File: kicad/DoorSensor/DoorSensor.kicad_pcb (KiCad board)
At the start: 2 copper layers, 29.7 x 38.6 mm, 11 parts, among them J1 AVR-ISP-6, J3 ADXL345 Module, U1 ATtiny44A-P, U2 NRF24L01_Breakout

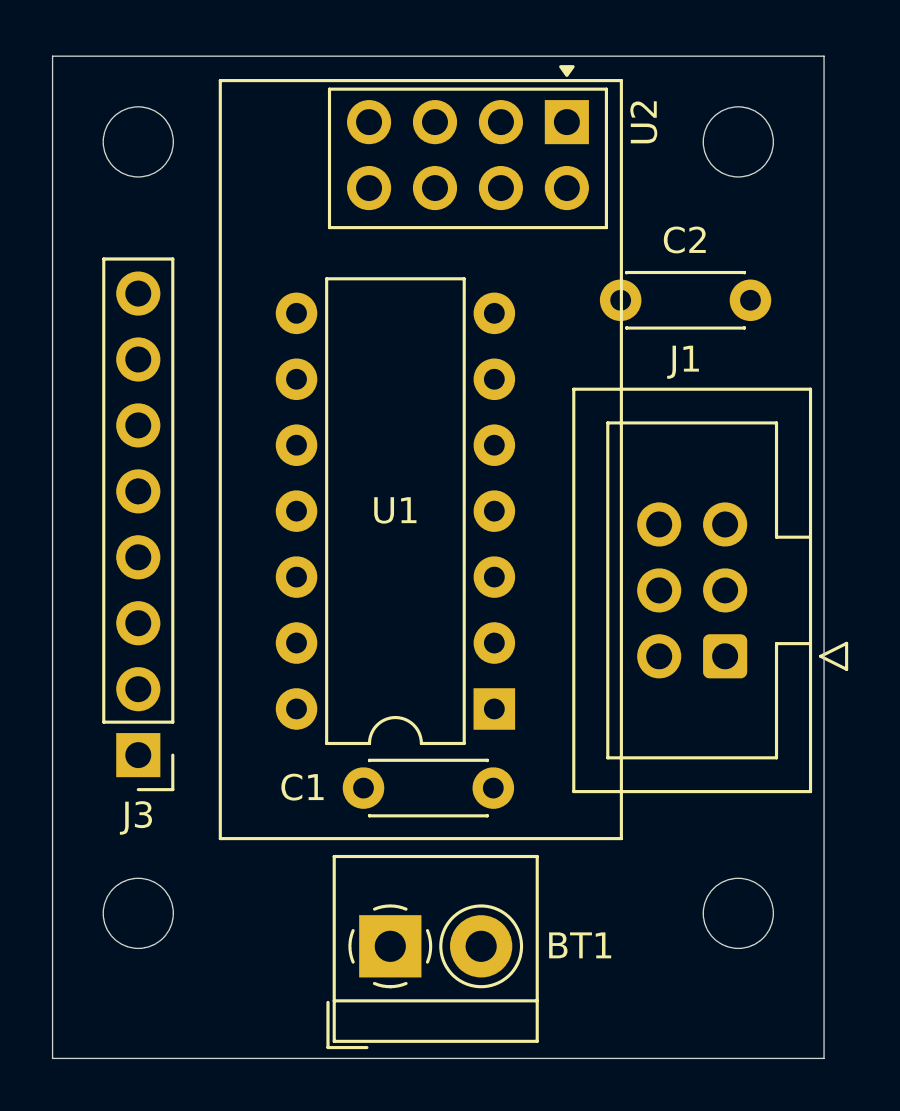
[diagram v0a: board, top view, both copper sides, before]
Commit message: Fixed WDT causing resets instead of triggering an interrupt
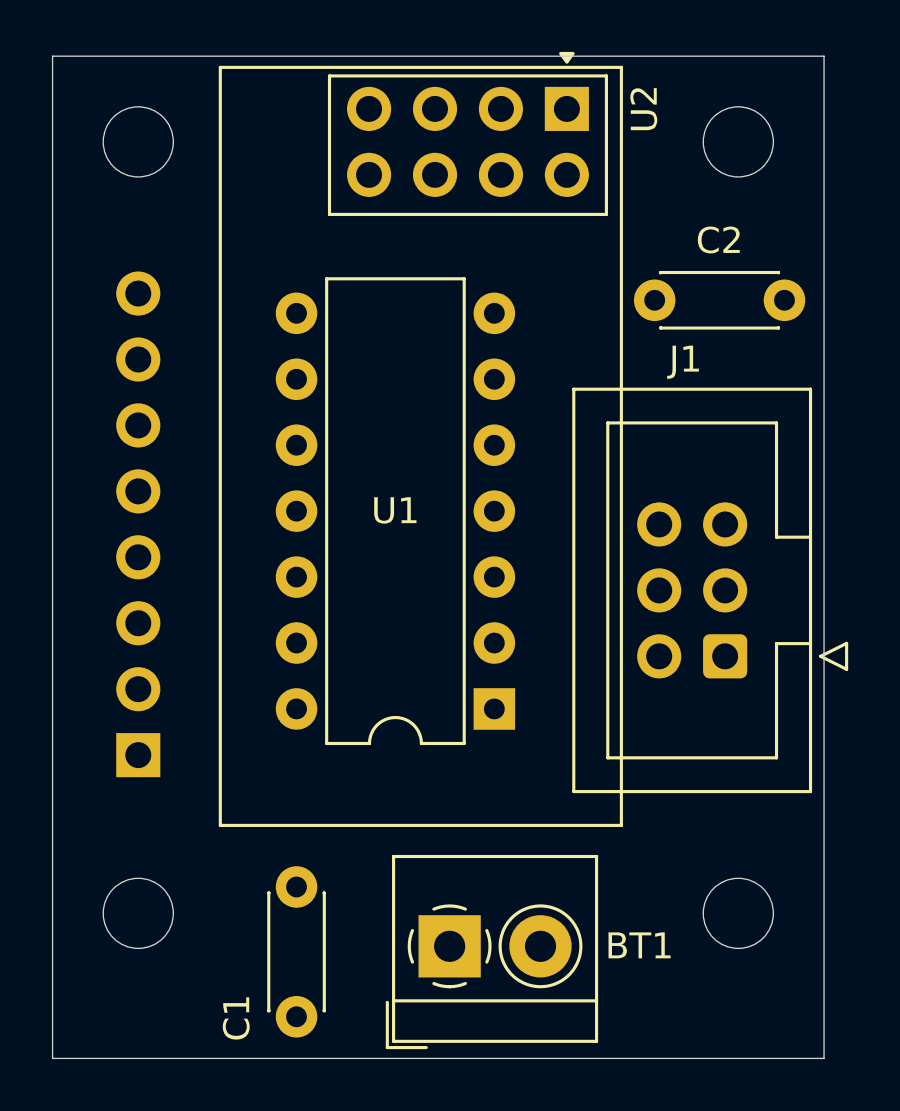
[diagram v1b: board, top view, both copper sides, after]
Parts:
- J3: moved to B.Cu
- moved C1 9.18 mm to (165.9, 120.3), turned to 90 degrees
- moved BT1 2.29 mm to (171.8, 117.6)
- moved C2 1.31 mm to (184.7, 92.7)
- moved U2 0.51 mm to (176.3, 85.3)
- turned J3 to 0 degrees
